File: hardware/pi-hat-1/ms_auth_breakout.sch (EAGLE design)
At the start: 20 parts, among them IC1 ULN2003AD

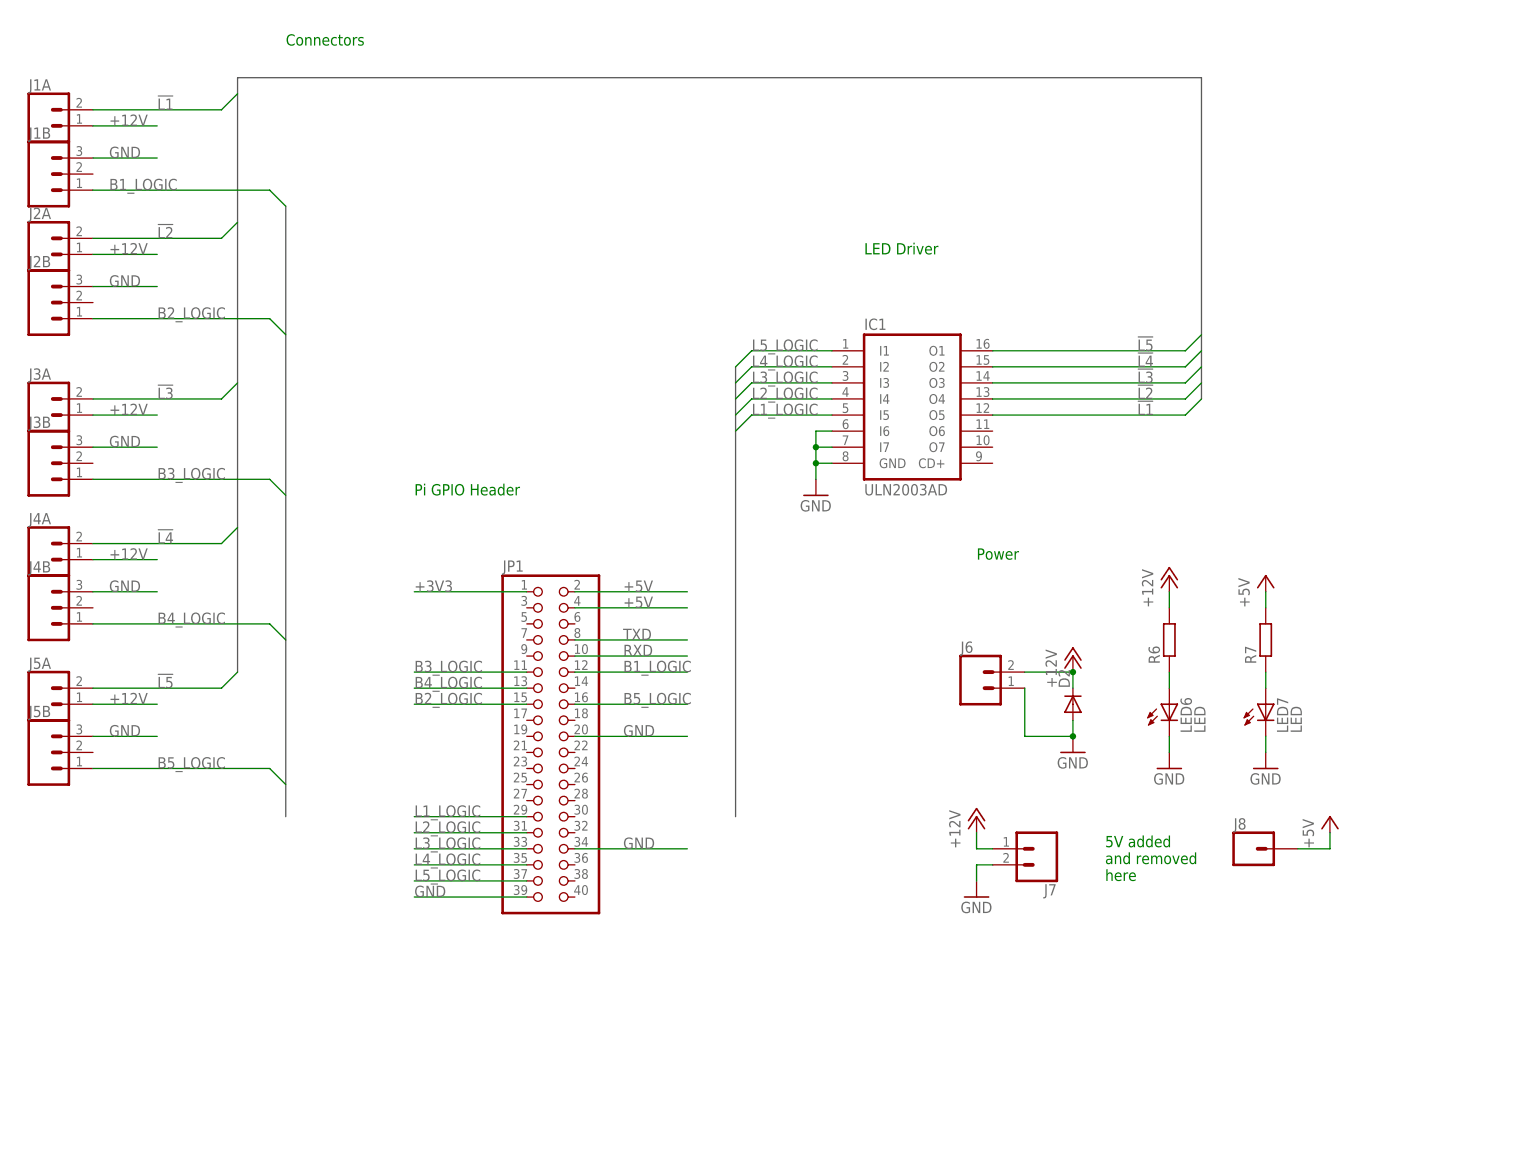
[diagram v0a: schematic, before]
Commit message: Board v0.2 sent to fab.
This now has 5 button headers, a dedicated PowerSwitch Tail header, and
a dedicated buzzer.  Buck converter has been moved onboard, and we
connect to a 3rd mounting hole for stability.  Since there's room, add a
barrel jack.

This version includes the pin number on silkscreen next to each item.

The 5-pin locking part isn't yet upstreamed to SparkFun's library.
The vector logo in ms-logo.lbr isn't updated in the schematic.
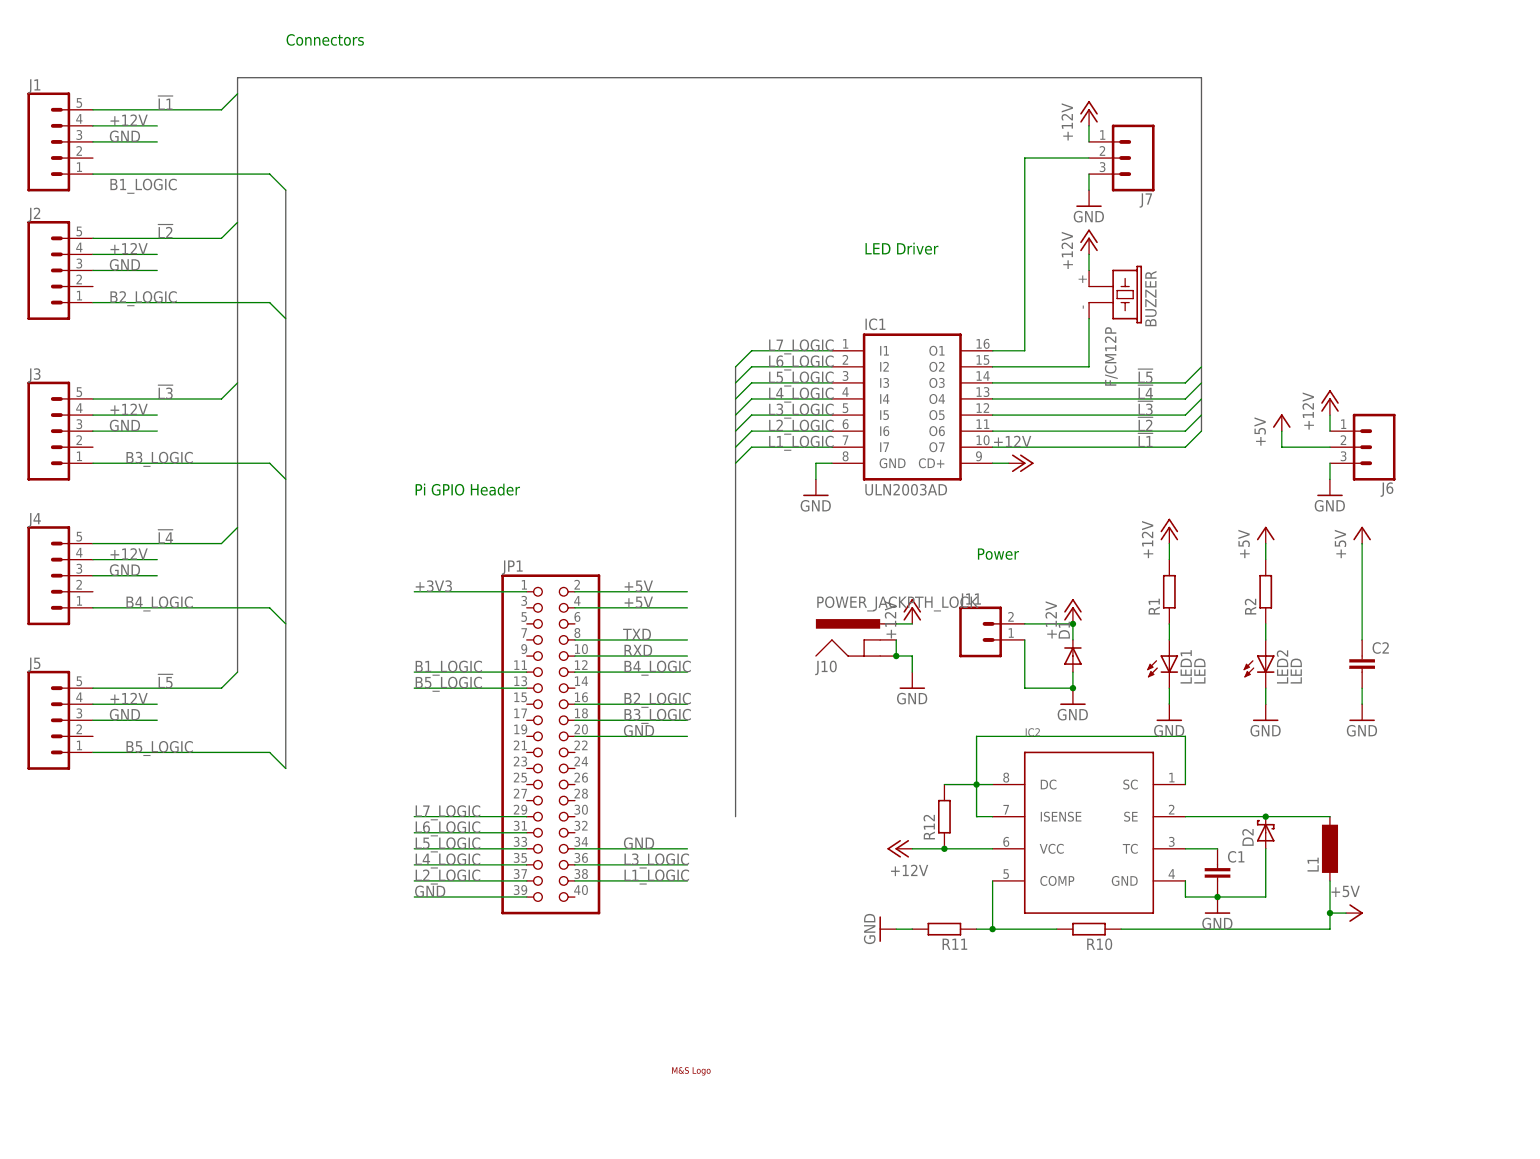
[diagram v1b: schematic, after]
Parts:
- removed J1A, J2A, J3A, J4A, J5A: (no value), SparkFun-Connectors:CONN_02POLAR_LOCK
- removed J1B, J2B, J3B, J4B, J5B: (no value), SparkFun-Connectors:CONN_03POLAR_LOCK
- removed J8: (no value), SparkFun-Connectors:CONN_01
- removed LED6, LED7: LED, Tim-Pretty:LED
- removed R6, R7: (no value), Tim-Pretty:R-EU_R0603
- added BUZZER: F/CM12P, buzzer:F/CM12P
- added C1: (no value), Tim-Pretty:C-EUC0603
- added C2: (no value), Tim-Pretty:C-EUC1206
- added D1: (no value), diode:DIODE-DO-214AC
- added IC2: MC3X063AD, mc3x063:MC3X063AD
- added J1, J2, J3, J4, J5: (no value), SparkFun-Connectors:CONN_05POLAR_LOCK
- added J10: POWER_JACKPTH_LOCK, SparkFun-Connectors:POWER_JACKPTH_LOCK
- added J11: (no value), SparkFun-Connectors:CONN_02POLAR_LOCK
- added L1: (no value), inductor-neosid:BS11
- added LED1, LED2: LED, Tim-Pretty:LED
- added R1, R10, R11, R2: (no value), Tim-Pretty:R-EU_R0603
- added R12: (no value), Tim-Pretty:R-EU_R1206
- added U$1: MS_LOGO, ms-logo:MS_LOGO
- D2: device diode:DIODE-DO-214AC -> diode:SCHOTTKY-DIODESMD
- J6: device SparkFun-Connectors:CONN_02POLAR_LOCK -> SparkFun-Connectors:CONN_03
- J7: device SparkFun-Connectors:CONN_02 -> SparkFun-Connectors:CONN_03POLAR_LOCK
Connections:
- new net L6_LOGIC: IC1.I2, JP1.31
- new net L7_LOGIC: IC1.I1, JP1.29
- new net N$1: D2.C, IC2.SE, L1.2
- new net N$2: BUZZER.2, IC1.O2
- new net N$3: IC2.COMP, R10.2, R11.1
- new net N$4: IC1.O1, J7.2
- new net N$5: IC2.DC, IC2.ISENSE, IC2.SC, R12.2
- new net N$8: C1.1, IC2.TC
- net !L1: now also IC1.O7, J1.5; no longer IC1.O5, J1A.2
- net !L2: now also IC1.O6, J2.5; no longer IC1.O4, J2A.2
- net !L3: now also IC1.O5, J3.5; no longer IC1.O3, J3A.2
- net !L4: now also IC1.O4, J4.5; no longer IC1.O2, J4A.2
- net !L5: now also IC1.O3, J5.5; no longer IC1.O1, J5A.2
- net +12V: now also BUZZER.1, D1.C, IC1.CD+, IC2.VCC, J1.4, J10.PWR, J11.2, J2.4, J3.4, J4.4, J5.4, J6.1, R1.2, R12.1; no longer D2.C, J1A.1, J2A.1, J3A.1, J4A.1, J5A.1, J6.2, R6.2
- net +5V: now also C2.1, J6.2, L1.1, R10.1, R2.2; no longer J8.1, R7.2
- net B1_LOGIC: now also J1.1, JP1.11; no longer J1B.1, JP1.12
- net B2_LOGIC: now also J2.1, JP1.16; no longer J2B.1, JP1.15
- net B3_LOGIC: now also J3.1, JP1.18; no longer J3B.1, JP1.11
- net B4_LOGIC: now also J4.1, JP1.12; no longer J4B.1, JP1.13
- net B5_LOGIC: now also J5.1, JP1.13; no longer J5B.1, JP1.16
- net GND: now also C1.2, C2.2, D1.A, IC2.GND, J1.3, J10.GND, J10.GNDBREAK, J11.1, J2.3, J3.3, J4.3, J5.3, J6.3, J7.3, LED1.C, LED2.C, R11.2; no longer IC1.I6, IC1.I7, J1B.3, J2B.3, J3B.3, J4B.3, J5B.3, J6.1, J7.2, LED6.C, LED7.C
- net L1_LOGIC: now also IC1.I7, JP1.38; no longer IC1.I5, JP1.29
- net L2_LOGIC: now also IC1.I6, JP1.37; no longer IC1.I4, JP1.31
- net L3_LOGIC: now also IC1.I5, JP1.36; no longer IC1.I3, JP1.33
- net L4_LOGIC: now also IC1.I4; no longer IC1.I2
- net L5_LOGIC: now also IC1.I3, JP1.33; no longer IC1.I1, JP1.37
- net N$11: now also LED1.A, R1.1; no longer LED6.A, R6.1
- net N$7: now also LED2.A, R2.1; no longer LED7.A, R7.1
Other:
- note removed: "5V added and removed here"

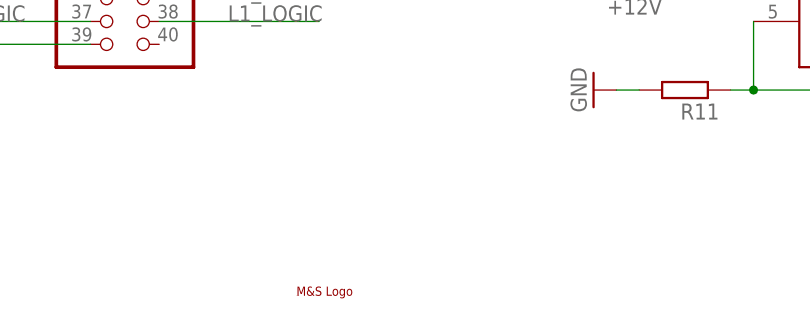
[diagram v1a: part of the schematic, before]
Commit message: Begin v0.3 of auth board
Improve 12V trace routing down the middle; swap to vector logo.
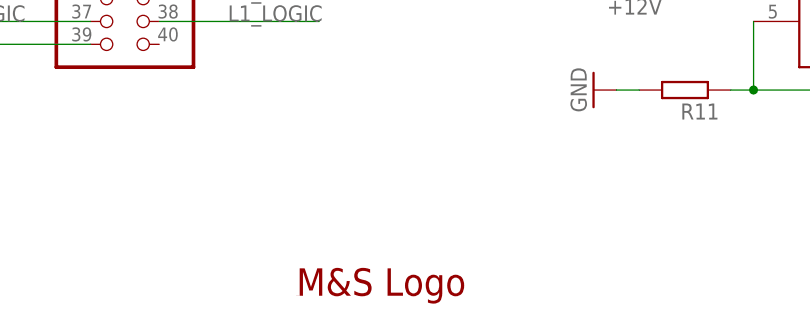
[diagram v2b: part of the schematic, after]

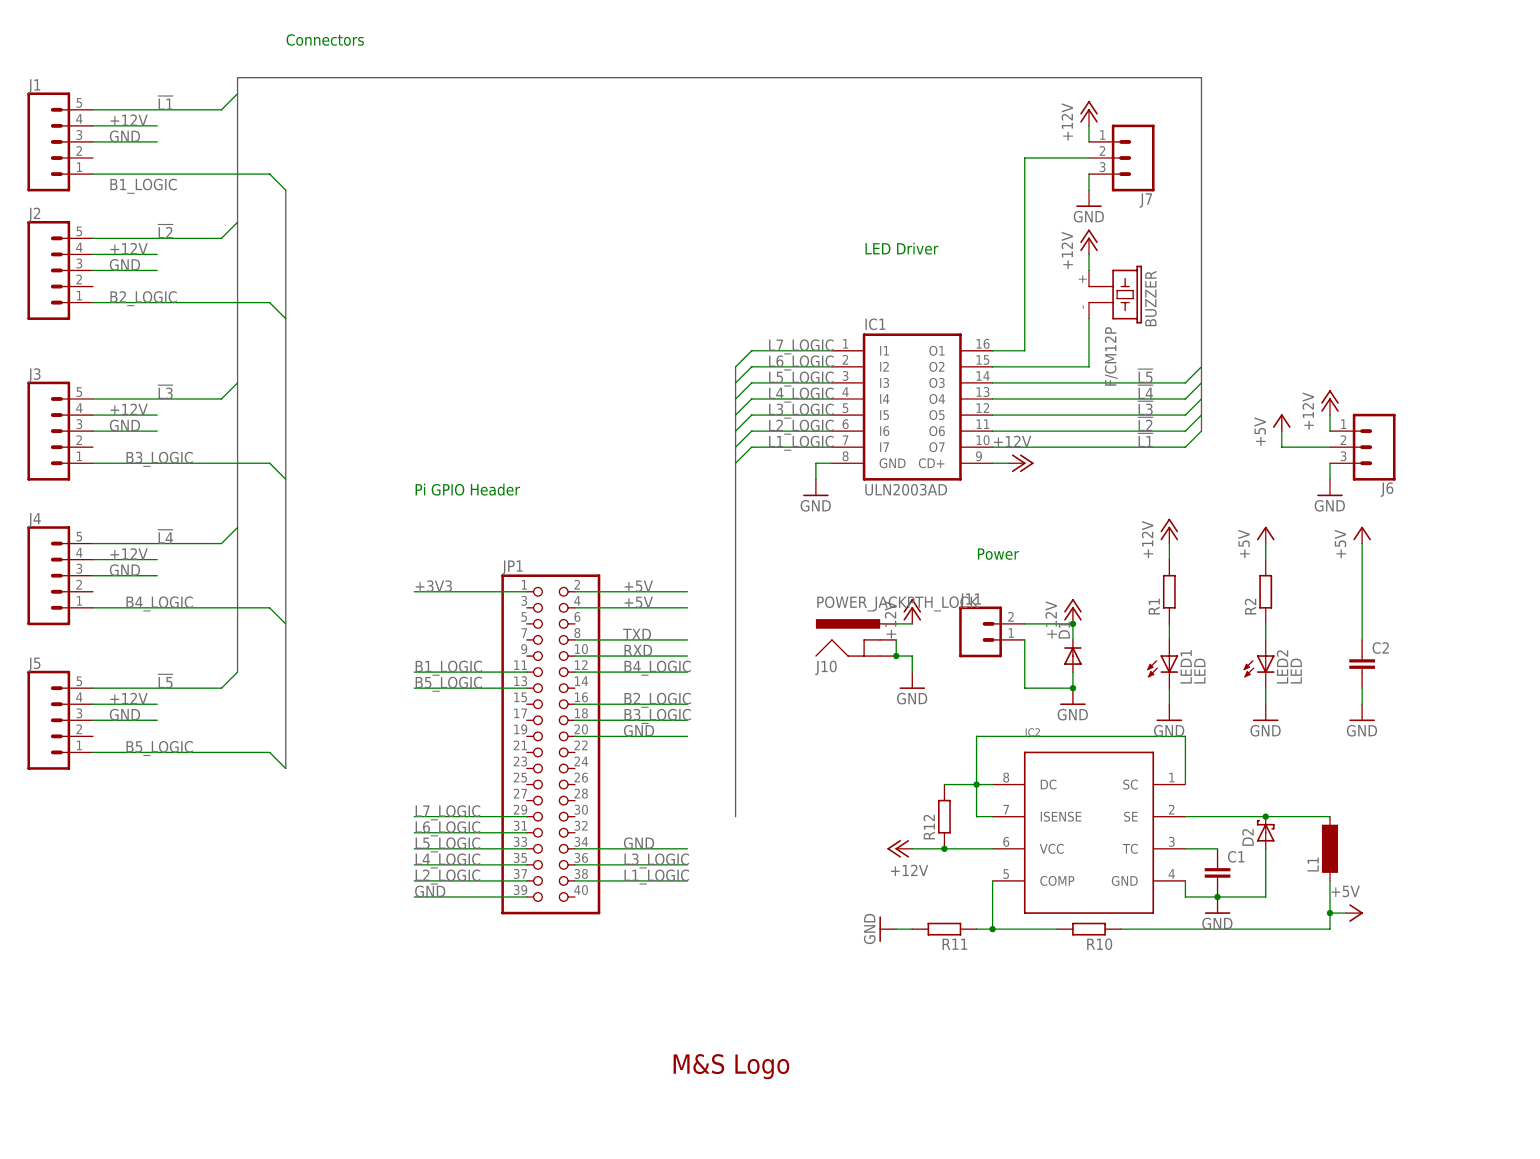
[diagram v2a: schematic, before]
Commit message: Getting ready to order pi-hat-1 v0.3
I re-routed this almost completely.  The area in the middle now makes a bit
more sense, and there's only one ground island that had to be reconnected.

* Switched back to buck module
* Found room for 6 button connectors again
* Added discrete RGB LED driver
* Added higher current output for inductive loads
  (ULN2003 maxes out at 500mA continuous, and I've popped a few trying
  solenoids without additional diodes)
* Pulldown resistors for the pins Robert discovered pulled high at boot
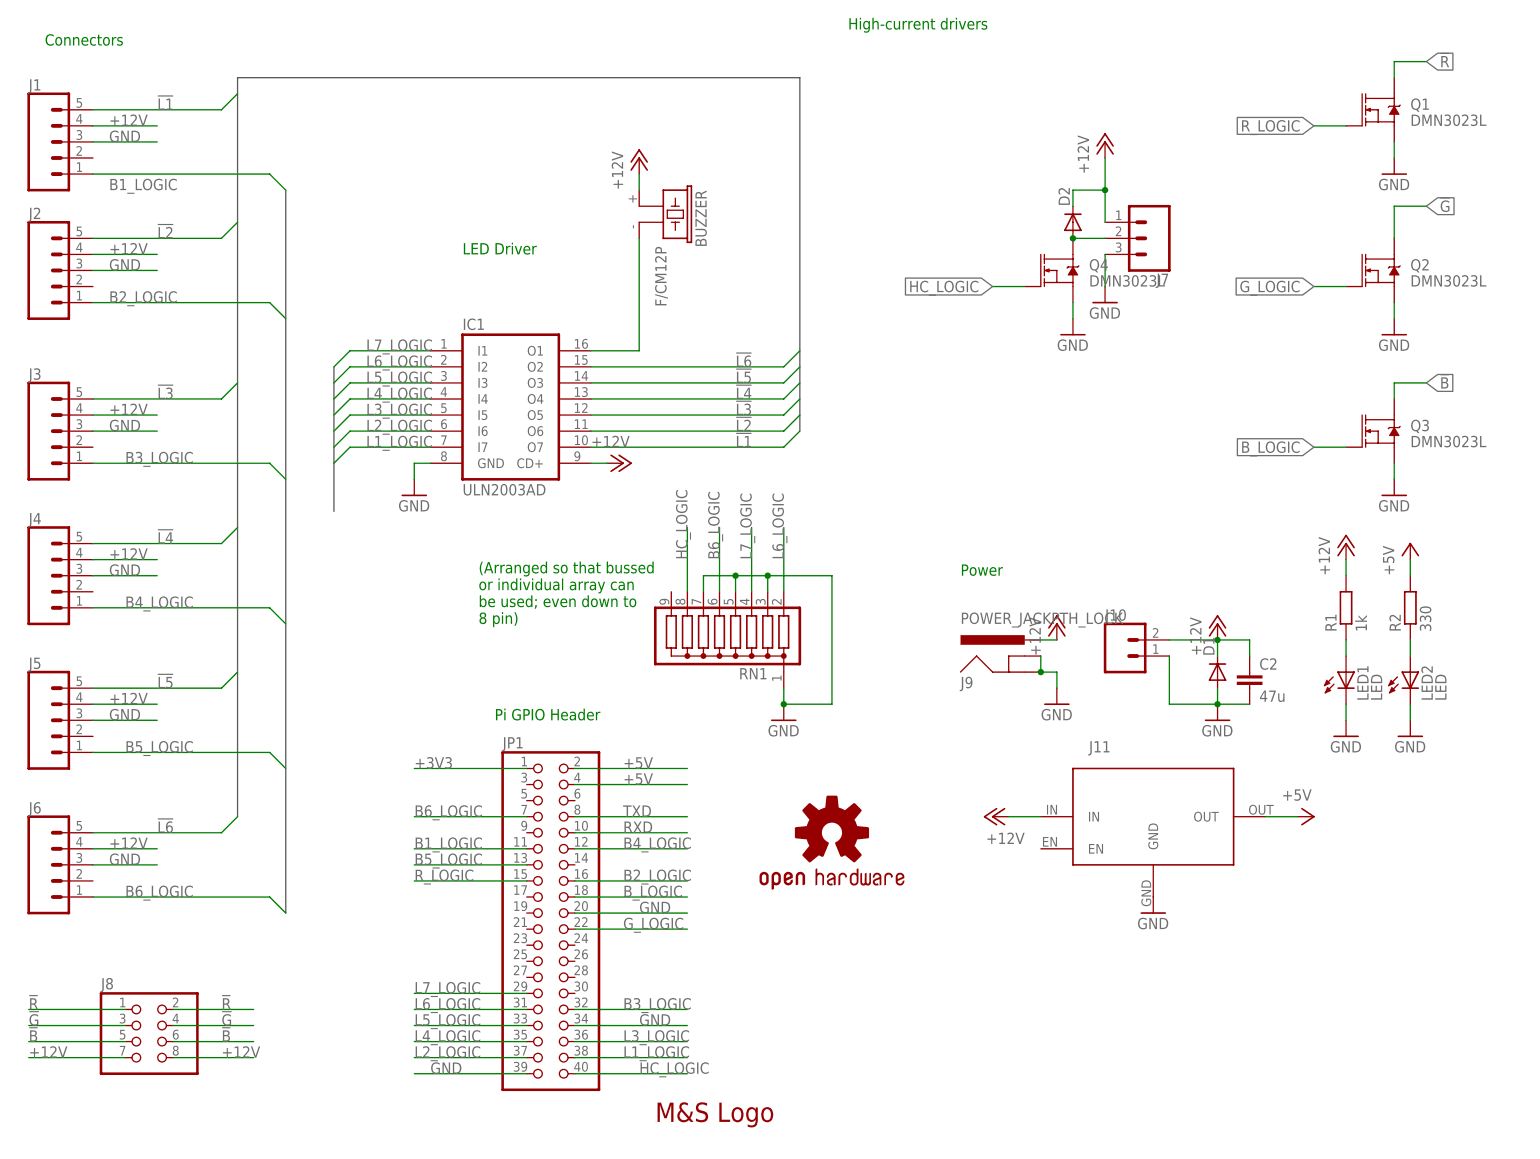
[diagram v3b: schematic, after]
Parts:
- removed C1: (no value), Tim-Pretty:C-EUC0603
- removed IC2: MC3X063AD, mc3x063:MC3X063AD
- removed L1: (no value), inductor-neosid:BS11
- removed R10, R11: (no value), Tim-Pretty:R-EU_R0603
- removed R12: (no value), Tim-Pretty:R-EU_R1206
- added J8: (no value), pinhead:PINHD-2X4
- added J9: POWER_JACKPTH_LOCK, SparkFun-Connectors:POWER_JACKPTH_LOCK
- added LOGO1: OSHW-LOGOM, SparkFun-Aesthetics:OSHW-LOGOM
- added Q1, Q2, Q3, Q4: DMN3023L, SparkFun-DiscreteSemi:MOSFET-NCH-AO3404A
- added RN1: (no value), resistor-sil:G08R
- C2: value (none) -> 47u
- D2: device diode:SCHOTTKY-DIODESMD -> diode:DIODE-DO-214AC
- J10: value POWER_JACKPTH_LOCK -> (none); device SparkFun-Connectors:POWER_JACKPTH_LOCK -> SparkFun-Connectors:CONN_02POLAR_LOCK
- J11: value (none) -> BUCK_MODULEHORIZONTAL; device SparkFun-Connectors:CONN_02POLAR_LOCK -> buck-module:BUCK_MODULEHORIZONTAL
- J6: device SparkFun-Connectors:CONN_03 -> SparkFun-Connectors:CONN_05POLAR_LOCK
- R1: value (none) -> 1k
- R2: value (none) -> 330
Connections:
- removed net N$1: D2.C, IC2.SE, L1.2
- removed net N$2: BUZZER.2, IC1.O2
- removed net N$3: IC2.COMP, R10.2, R11.1
- removed net N$5: IC2.DC, IC2.ISENSE, IC2.SC, R12.2
- removed net N$8: C1.1, IC2.TC
- new net !B: J8.5, J8.6, Q3.D
- new net !G: J8.3, J8.4, Q2.D
- new net !L6: IC1.O2, J6.5
- new net !R: J8.1, J8.2, Q1.D
- new net B6_LOGIC: J6.1, JP1.7, RN1.6
- new net B_LOGIC: JP1.18, Q3.G
- new net G_LOGIC: JP1.22, Q2.G
- new net HC_LOGIC: JP1.40, Q4.G, RN1.8
- new net N$13: BUZZER.2, IC1.O1
- new net R_LOGIC: JP1.15, Q1.G
- net +12V: now also C2.1, D2.C, J10.2, J11.IN, J6.4, J8.7, J8.8, J9.PWR; no longer IC2.VCC, J10.PWR, J11.2, J6.1, R12.1
- net +5V: now also J11.OUT; no longer C2.1, J6.2, L1.1, R10.1
- net B3_LOGIC: now also JP1.32; no longer JP1.18
- net GND: now also J10.1, J11.GND, J9.GND, J9.GNDBREAK, Q1.S, Q2.S, Q3.S, Q4.S, RN1.1, RN1.3, RN1.5, RN1.7; no longer C1.2, D2.A, IC2.GND, J10.GND, J10.GNDBREAK, J11.1, R11.2
- net L6_LOGIC: now also RN1.2
- net L7_LOGIC: now also RN1.4
- net N$4: now also D2.A, Q4.D; no longer IC1.O1
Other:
- note added: "(Arranged so that bussed or individual array can be used; even down to 8 pin)"
- note added: "High-current drivers"
- moved on the sheet: BUZZER, C2, D1, IC1, J10, J7, JP1, LED1, LED2, R1, R2
